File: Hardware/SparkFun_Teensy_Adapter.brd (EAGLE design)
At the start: 21 parts, among them U1 5V

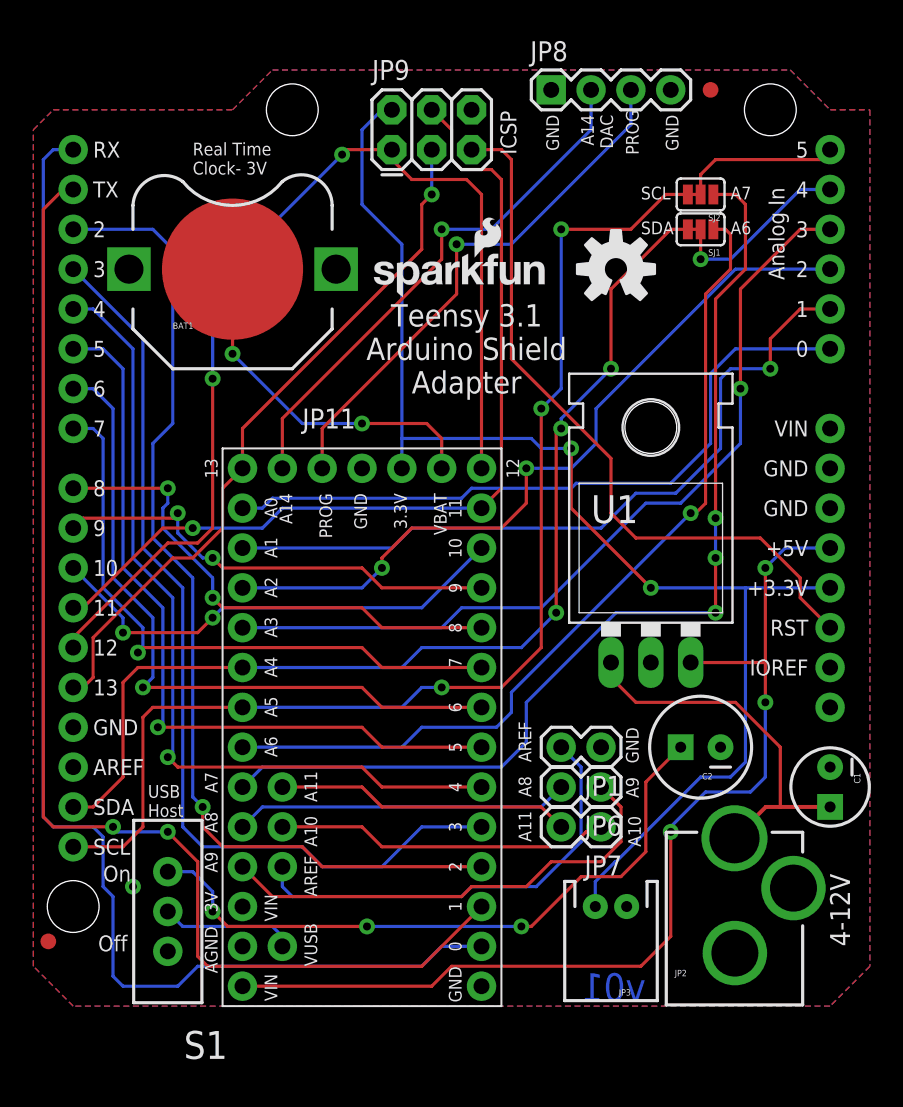
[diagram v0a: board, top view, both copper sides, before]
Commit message: Fixing QC checklist issues
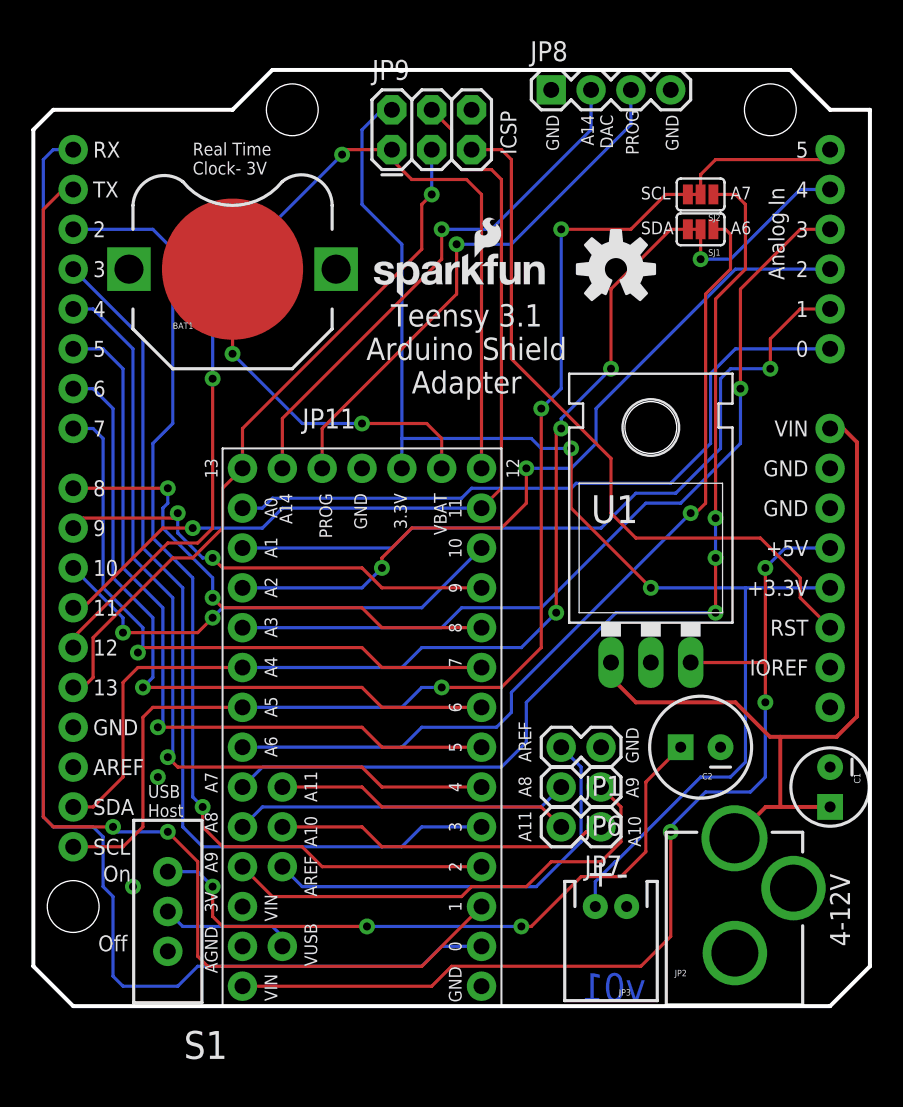
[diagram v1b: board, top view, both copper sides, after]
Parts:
- removed FID1, FID2: FIDUCIAL1X2, SparkFun-Aesthetics:FIDUCIAL-1X2
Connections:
- removed net N$2: JP10.VIN
- net VRAW: now also JP10.VIN
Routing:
- net VRAW: track 24.3 -> 49.7 mm
- net AREF: track 28.6 -> 27.3 mm
- net D3: track 59.6 -> 58.6 mm
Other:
- board outline added: 53.3 x 59.7 mm
- board text added: "+"
- board text added: "-"
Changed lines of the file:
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@@
 <layer number="45" name="Holes" color="7" fill="1" visible="yes" active="yes"/>
 <layer number="46" name="Milling" color="3" fill="1" visible="no" active="yes"/>
-<layer number="47" name="Measures" color="7" fill="1" visible="yes" active="yes"/>
+<layer number="47" name="Measures" color="7" fill="1" visible="no" active="yes"/>
 <layer number="48" name="Document" color="7" fill="1" visible="no" active="yes"/>
 <layer number="49" name="Reference" color="7" fill="1" visible="no" active="yes"/>
@@
 <layer number="223" name="223bmp" color="24" fill="1" visible="no" active="no"/>
 <layer number="224" name="224bmp" color="25" fill="1" visible="no" active="no"/>
-<layer number="225" name="225bmp" color="7" fill="1" visible="yes" active="yes"/>
-<layer number="226" name="226bmp" color="7" fill="1" visible="yes" active="yes"/>
-<layer number="227" name="227bmp" color="7" fill="1" visible="yes" active="yes"/>
-<layer number="228" name="228bmp" color="7" fill="1" visible="yes" active="yes"/>
-<layer number="229" name="229bmp" color="7" fill="1" visible="yes" active="yes"/>
-<layer number="230" name="230bmp" color="7" fill="1" visible="yes" active="yes"/>
-<layer number="231" name="231bmp" color="7" fill="1" visible="yes" active="yes"/>
+<layer number="225" name="225bmp" color="7" fill="1" visible="no" active="yes"/>
+<layer number="226" name="226bmp" color="7" fill="1" visible="no" active="yes"/>
+<layer number="227" name="227bmp" color="7" fill="1" visible="no" active="yes"/>
+<layer number="228" name="228bmp" color="7" fill="1" visible="no" active="yes"/>
+<layer number="229" name="229bmp" color="7" fill="1" visible="no" active="yes"/>
+<layer number="230" name="230bmp" color="7" fill="1" visible="no" active="yes"/>
+<layer number="231" name="231bmp" color="7" fill="1" visible="no" active="yes"/>
 <layer number="248" name="Housing" color="7" fill="1" visible="no" active="yes"/>
 <layer number="249" name="Edge" color="7" fill="1" visible="no" active="yes"/>
@@
 <text x="6.6675" y="20.0025" size="1.016" layer="21" font="vector" ratio="15">Off</text>
 <text x="33.3375" y="70.8025" size="1.016" layer="21" font="vector" ratio="15" rot="R90">ICSP</text>
+<wire x1="2.54" y1="19.05" x2="5.08" y2="16.51" width="0.254" layer="20"/>
+<wire x1="5.08" y1="16.51" x2="53.34" y2="16.51" width="0.254" layer="20"/>
+<wire x1="53.34" y1="16.51" x2="55.88" y2="19.05" width="0.254" layer="20"/>
+<wire x1="55.88" y1="19.05" x2="55.88" y2="73.66" width="0.254" layer="20"/>
+<wire x1="55.88" y1="73.66" x2="53.34" y2="73.66" width="0.254" layer="20"/>
+<wire x1="53.34" y1="73.66" x2="50.8" y2="76.2" width="0.254" layer="20"/>
+<wire x1="50.8" y1="76.2" x2="17.78" y2="76.2" width="0.254" layer="20"/>
+<wire x1="17.78" y1="76.2" x2="15.24" y2="73.66" width="0.254" layer="20"/>
+<wire x1="15.24" y1="73.66" x2="3.81" y2="73.66" width="0.254" layer="20"/>
+<wire x1="3.81" y1="73.66" x2="2.54" y2="72.39" width="0.254" layer="20"/>
+<wire x1="2.54" y1="72.39" x2="2.54" y2="19.05" width="0.254" layer="20"/>
+<text x="34.29" y="32.0675" size="0.8128" layer="22" font="vector" ratio="15" rot="MR90" align="top-left">AREF</text>
+<text x="34.29" y="29.845" size="0.8128" layer="22" font="vector" ratio="15" rot="MR90" align="top-left">A8</text>
+<text x="34.29" y="26.9875" size="0.8128" layer="22" font="vector" ratio="15" rot="MR90" align="top-left">A11</text>
+<text x="41.275" y="26.67" size="0.8128" layer="22" font="vector" ratio="15" rot="MR90" align="top-left">A10</text>
+<text x="40.3225" y="31.115" size="0.8128" layer="22" font="vector" ratio="15" rot="MR270" align="top-left">A9</text>
+<text x="40.3225" y="34.29" size="0.8128" layer="22" font="vector" ratio="15" rot="MR270" align="top-left">GND</text>
+<text x="35.2425" y="73.3425" size="0.8128" layer="22" font="vector" ratio="15" rot="MR270" align="top-left">GND</text>
+<text x="37.465" y="73.3425" size="0.8128" layer="22" font="vector" ratio="15" rot="MR270" align="top-left">A14
+DAC</text>
+<text x="40.3225" y="73.66" size="0.8128" layer="22" font="vector" ratio="15" rot="MR270" align="top-left">PROG</text>
+<text x="42.8625" y="73.3425" size="0.8128" layer="22" font="vector" ratio="15" rot="MR270" align="top-left">GND</text>
+<text x="37.7825" y="24.13" size="1.778" layer="21" font="vector" ratio="15">+</text>
+<text x="39.6875" y="24.13" size="1.778" layer="21" font="vector" ratio="15">-</text>
 </plain>
 <attributes>
@@
 </autorouter>
 <elements>
-<element name="FID1" library="SparkFun-Aesthetics" package="FIDUCIAL-1X2" value="FIDUCIAL1X2" x="45.72" y="74.93"/>
-<element name="FID2" library="SparkFun-Aesthetics" package="FIDUCIAL-1X2" value="FIDUCIAL1X2" x="3.4925" y="20.6375"/>
 <element name="FRAME1" library="SparkFun-Aesthetics" package="CREATIVE_COMMONS" value="" x="3.81" y="-10.16">
 <attribute name="VERSION" value="v01" x="41.5925" y="16.8275" size="1.778" layer="16" font="vector" ratio="15" rot="MR0"/>
@@
 <contactref element="C2" pad="2"/>
 <via x="8.89" y="24.13" extent="1-16" drill="0.508"/>
+<via x="10.4775" y="31.115" extent="1-16" drill="0.508"/>
 </signal>
 <signal name="RX">
@@
 <contactref element="JP11" pad="3"/>
 <wire x1="31.115" y1="27.94" x2="27.305" y2="27.94" width="0.2032" layer="16"/>
-<wire x1="27.305" y1="27.94" x2="24.765" y2="25.4" width="0.2032" layer="16"/>
-<wire x1="24.765" y1="25.4" x2="20.955" y2="25.4" width="0.2032" layer="16"/>
-<wire x1="20.955" y1="25.4" x2="19.685" y2="26.67" width="0.2032" layer="16"/>
 <wire x1="9.525" y1="45.72" x2="9.525" y2="59.055" width="0.2032" layer="16"/>
-<wire x1="19.685" y1="26.67" x2="13.335" y2="26.67" width="0.2032" layer="16"/>
 <wire x1="12.065" y1="27.94" x2="12.065" y2="43.18" width="0.2032" layer="16"/>
 <wire x1="12.065" y1="43.18" x2="9.525" y2="45.72" width="0.2032" layer="16"/>
 <wire x1="13.335" y1="26.67" x2="12.065" y2="27.94" width="0.2032" layer="16"/>
 <wire x1="5.08" y1="63.5" x2="9.525" y2="59.055" width="0.2032" layer="16"/>
+<wire x1="13.335" y1="26.67" x2="26.035" y2="26.67" width="0.2032" layer="16"/>
+<wire x1="26.035" y1="26.67" x2="27.305" y2="27.94" width="0.2032" layer="16"/>
 </signal>
 <signal name="D4">
@@
 <contactref element="JP11" pad="AREF"/>
 <contactref element="JP1" pad="2"/>
-<wire x1="18.415" y1="25.4" x2="18.415" y2="24.13" width="0.2032" layer="16"/>
-<wire x1="18.415" y1="24.13" x2="19.05" y2="23.495" width="0.2032" layer="16"/>
-<wire x1="19.05" y1="23.495" x2="29.845" y2="23.495" width="0.2032" layer="16"/>
-<wire x1="29.845" y1="23.495" x2="30.48" y2="24.13" width="0.2032" layer="16"/>
-<wire x1="30.48" y1="24.13" x2="34.6075" y2="24.13" width="0.2032" layer="16"/>
 <wire x1="34.6075" y1="24.13" x2="37.465" y2="26.9875" width="0.2032" layer="16"/>
 <wire x1="37.465" y1="26.9875" x2="37.465" y2="31.75" width="0.2032" layer="16"/>
 <wire x1="37.465" y1="31.75" x2="36.195" y2="33.02" width="0.2032" layer="16"/>
+<wire x1="34.6075" y1="24.13" x2="19.685" y2="24.13" width="0.2032" layer="16"/>
+<wire x1="19.685" y1="24.13" x2="18.415" y2="25.4" width="0.2032" layer="16"/>
 </signal>
 <signal name="RTC_BATT">
@@
 <wire x1="50.165" y1="29.21" x2="49.2412" y2="29.21" width="0.254" layer="1"/>
 <wire x1="49.2412" y1="29.21" x2="47.244" y2="27.2128" width="0.254" layer="1"/>
-<wire x1="39.37" y1="38.4175" x2="39.37" y2="37.465" width="0.2032" layer="1"/>
-<wire x1="39.37" y1="37.465" x2="40.9575" y2="35.8775" width="0.2032" layer="1"/>
-<wire x1="40.9575" y1="35.8775" x2="47.3075" y2="35.8775" width="0.2032" layer="1"/>
-<wire x1="47.3075" y1="35.8775" x2="50.165" y2="33.02" width="0.2032" layer="1"/>
-<wire x1="50.165" y1="33.02" x2="50.165" y2="29.21" width="0.2032" layer="1"/>
+<wire x1="39.37" y1="38.4175" x2="39.37" y2="37.465" width="0.254" layer="1"/>
+<wire x1="39.37" y1="37.465" x2="40.9575" y2="35.8775" width="0.254" layer="1"/>
+<wire x1="40.9575" y1="35.8775" x2="47.3075" y2="35.8775" width="0.254" layer="1"/>
+<wire x1="50.165" y1="33.6804" x2="50.165" y2="29.21" width="0.254" layer="1"/>
+<contactref element="JP10" pad="VIN"/>
+<wire x1="53.34" y1="53.34" x2="54.1782" y2="53.34" width="0.254" layer="1"/>
+<wire x1="54.1782" y1="53.34" x2="55.0545" y2="52.4637" width="0.254" layer="1"/>
+<wire x1="55.0545" y1="52.4637" x2="55.0545" y2="34.9758" width="0.254" layer="1"/>
+<wire x1="55.0545" y1="34.9758" x2="53.7591" y2="33.6804" width="0.254" layer="1"/>
+<wire x1="53.7591" y1="33.6804" x2="50.165" y2="33.6804" width="0.254" layer="1"/>
+<wire x1="50.165" y1="33.6804" x2="49.5046" y2="33.6804" width="0.254" layer="1"/>
+<wire x1="49.5046" y1="33.6804" x2="47.3075" y2="35.8775" width="0.254" layer="1"/>
 </signal>
 <signal name="5V">
@@
 <wire x1="49.2125" y1="31.115" x2="49.2125" y2="35.8775" width="0.2032" layer="16"/>
 </signal>
-<signal name="N$2">
-<contactref element="JP10" pad="VIN"/>
-</signal>
 <signal name="A8">
 <contactref element="JP11" pad="22"/>
@@
 <wire x1="41.5925" y1="26.3525" x2="41.5925" y2="30.7975" width="0.2032" layer="1"/>
 <wire x1="41.5925" y1="30.7975" x2="43.815" y2="33.02" width="0.2032" layer="1"/>
-<wire x1="23.8125" y1="21.59" x2="14.9225" y2="21.59" width="0.2032" layer="1"/>
-<via x="13.97" y="22.5425" extent="1-16" drill="0.508"/>
-<wire x1="12.7" y1="25.0825" x2="11.1125" y2="25.0825" width="0.2032" layer="16"/>
-<wire x1="14.9225" y1="21.59" x2="13.97" y2="22.5425" width="0.2032" layer="1"/>
-<wire x1="12.7" y1="25.0825" x2="13.97" y2="23.8125" width="0.2032" layer="16"/>
-<wire x1="13.97" y1="23.8125" x2="13.97" y2="22.5425" width="0.2032" layer="16"/>
+<wire x1="23.8125" y1="21.59" x2="14.605" y2="21.59" width="0.2032" layer="1"/>
+<via x="13.97" y="24.13" extent="1-16" drill="0.508"/>
+<wire x1="13.0175" y1="25.0825" x2="11.1125" y2="25.0825" width="0.2032" layer="16"/>
+<wire x1="13.0175" y1="25.0825" x2="13.97" y2="24.13" width="0.2032" layer="16"/>
+<wire x1="14.605" y1="21.59" x2="13.97" y2="22.225" width="0.2032" layer="1"/>
+<wire x1="13.97" y1="22.225" x2="13.97" y2="24.13" width="0.2032" layer="1"/>
 </signal>
 </signals>

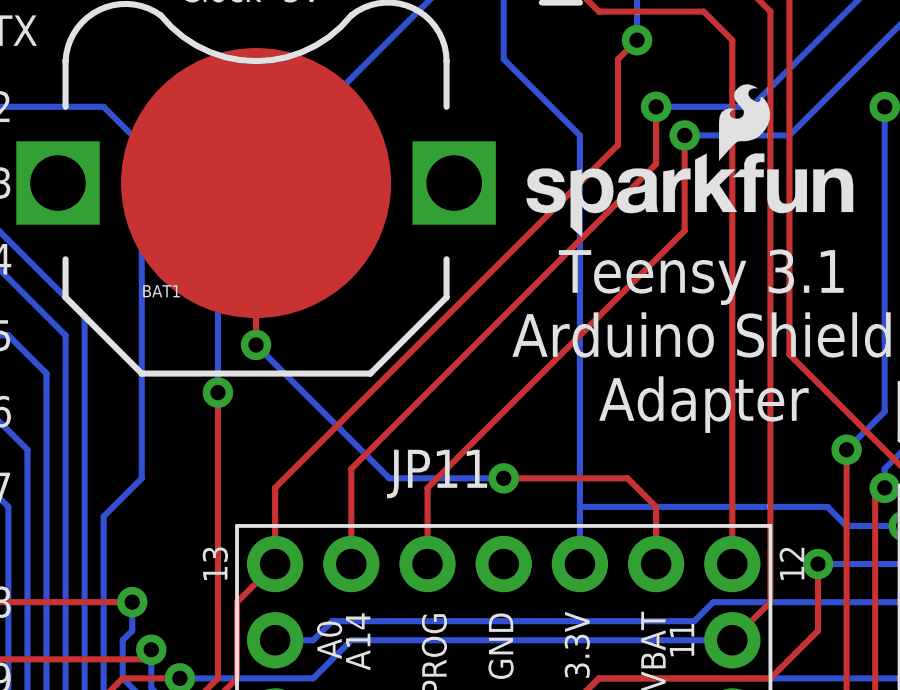
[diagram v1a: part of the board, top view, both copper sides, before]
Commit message: Fixing battery connections
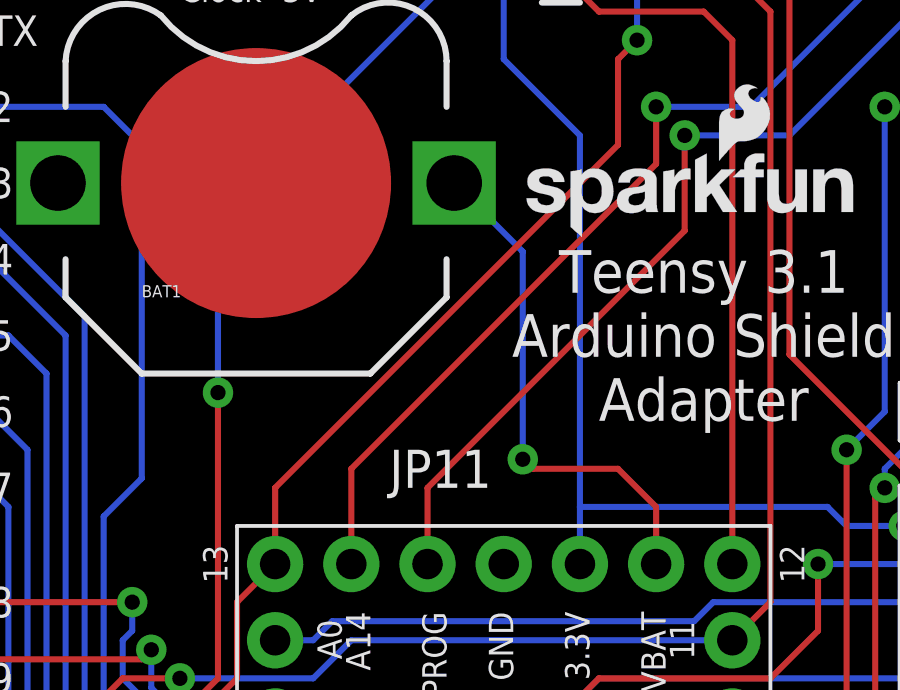
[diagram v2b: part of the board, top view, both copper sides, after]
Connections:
- net GND: now also BAT1.GND; no longer BAT1.VCC@1
- net RTC_BATT: now also BAT1.VCC@1; no longer BAT1.GND
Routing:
- net RTC_BATT: track 22.9 -> 17.2 mm, vias 2 -> 1
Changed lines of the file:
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@@
 <setting verticaltext="up"/>
 </settings>
-<grid distance="0.0125" unitdist="inch" unit="inch" style="lines" multiple="1" display="yes" altdistance="0.005" altunitdist="inch" altunit="inch"/>
+<grid distance="0.025" unitdist="inch" unit="inch" style="lines" multiple="1" display="yes" altdistance="0.005" altunitdist="inch" altunit="inch"/>
 <layers>
 <layer number="1" name="Top" color="4" fill="1" visible="yes" active="yes"/>
@@
 <contactref element="JP8" pad="1"/>
 <contactref element="JP8" pad="4"/>
-<contactref element="BAT1" pad="VCC@1"/>
 <contactref element="JP1" pad="1"/>
 <contactref element="U1" pad="GND"/>
@@
 <via x="8.89" y="24.13" extent="1-16" drill="0.508"/>
 <via x="10.4775" y="31.115" extent="1-16" drill="0.508"/>
+<contactref element="BAT1" pad="GND"/>
 </signal>
 <signal name="RX">
@@
 <signal name="RTC_BATT">
 <contactref element="JP11" pad="VBAT"/>
-<contactref element="BAT1" pad="GND"/>
+<via x="24.13" y="54.2925" extent="1-16" drill="0.508"/>
+<contactref element="BAT1" pad="VCC@1"/>
 <wire x1="28.575" y1="50.8" x2="28.575" y2="52.705" width="0.2032" layer="1"/>
-<wire x1="28.575" y1="52.705" x2="27.6225" y2="53.6575" width="0.2032" layer="1"/>
-<wire x1="27.6225" y1="53.6575" x2="23.495" y2="53.6575" width="0.2032" layer="1"/>
-<via x="23.495" y="53.6575" extent="1-16" drill="0.508"/>
-<wire x1="23.495" y1="53.6575" x2="19.685" y2="53.6575" width="0.2032" layer="16"/>
-<wire x1="19.685" y1="53.6575" x2="15.24" y2="58.1025" width="0.2032" layer="16"/>
-<via x="15.24" y="58.1025" extent="1-16" drill="0.508"/>
-<wire x1="15.24" y1="58.1025" x2="15.24" y2="63.5" width="0.2032" layer="1"/>
+<wire x1="28.575" y1="52.705" x2="27.305" y2="53.975" width="0.2032" layer="1"/>
+<wire x1="27.305" y1="53.975" x2="24.4475" y2="53.975" width="0.2032" layer="1"/>
+<wire x1="24.4475" y1="53.975" x2="24.13" y2="54.2925" width="0.2032" layer="1"/>
+<wire x1="24.13" y1="54.2925" x2="24.13" y2="61.214" width="0.2032" layer="16"/>
+<wire x1="24.13" y1="61.214" x2="21.844" y2="63.5" width="0.2032" layer="16"/>
 </signal>
 <signal name="VRAW">
